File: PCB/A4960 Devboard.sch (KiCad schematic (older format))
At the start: 59 parts, among them IC1 ATMEGA8-AI, P1 CONN_02X03, P2 CONN_01X02, P3 CONN_01X03, P4 CONN_01X03, Q1 SIRA00DP-T1-GE3, Q2 SIRA00DP-T1-GE3, Q3 SIRA00DP-T1-GE3, Q4 SIRA00DP-T1-GE3, Q5 SIRA00DP-T1-GE3, Q6 SIRA00DP-T1-GE3, U2 A4960, Y1 16MHz

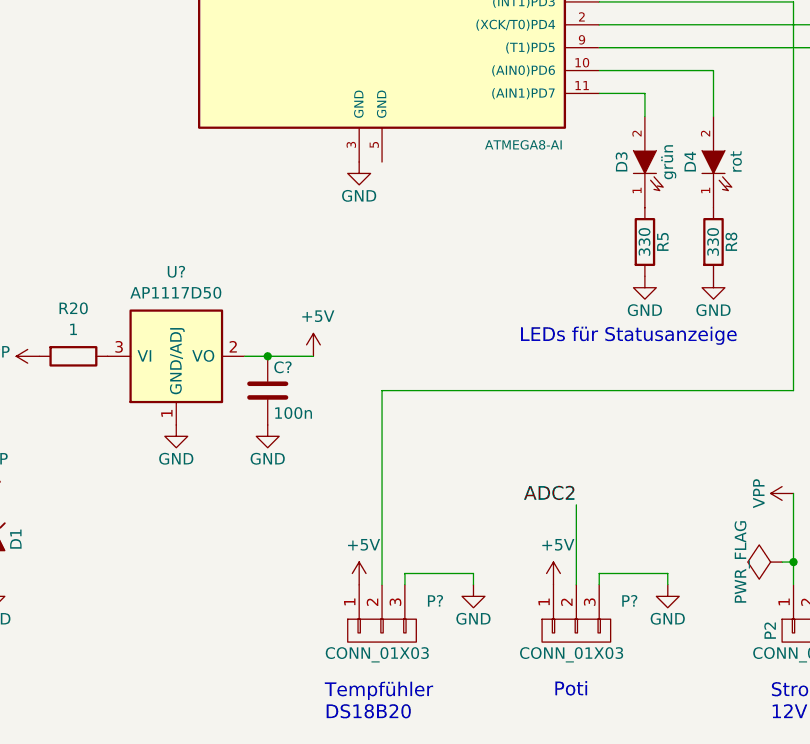
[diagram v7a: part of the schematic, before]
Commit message: Pullup für DS18B20 Tempsensor hinzugefügt.
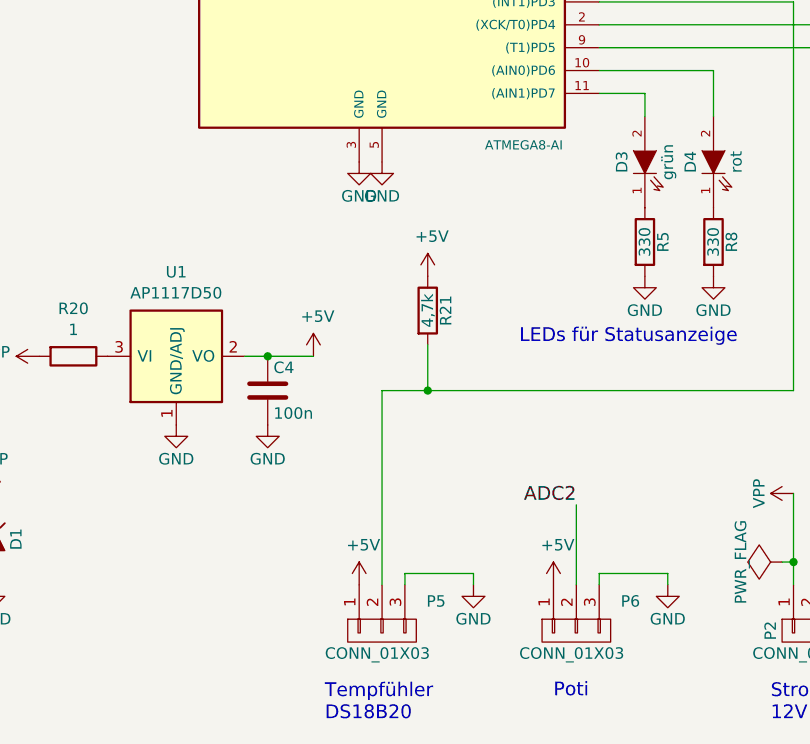
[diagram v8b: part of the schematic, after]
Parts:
- added R21: 4,7k, Resistors_SMD:R_0603, symbol R
- P5, P6: renamed from P?; footprint (none) -> Pin_Headers:Pin_Header_Straight_1x03
- R20: footprint (none) -> Resistors_SMD:R_0805
- U1: renamed from U?; footprint (none) -> TO_SOT_Packages_SMD:SOT-223
- gave numbers to parts that had none: 1
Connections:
- net +5V: now also R21.1
- net GND: now also IC1.5 (GND)
- net at IC1.1 ((INT1)PD3), P5.2 (P2): now also R21.2
